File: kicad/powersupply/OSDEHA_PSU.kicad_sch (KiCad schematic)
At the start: 62 parts, among them J1 340 VAC / 220 mA, J10 COLEMANREG-RIGHT-2, J11 HV-L, J12 HV-R, J13 HEATERS-LEFT, J14 HEATERS-RIGHT, J15 Stator bias, J2 340 VAC / 220 mA, J3 420 VAC / 75 mA, J4 9 VAC / 4.5 A, J5 9.5 VAC / 4.5 A, J6 9.5 VAC / 4.5 A, J7 COLEMANREG-LEFT-1, J8 COLEMANREG-LEFT-2, J9 COLEMANREG-RIGHT-1, K1 Relay_DPST-NO, Q1 BD138, Q2 10M90S, U1 LM1085-ADJ, U2 NE555P

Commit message: up
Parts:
- J5, J6: value 9.5 VAC / 4.5 A -> 10.5 VAC / 4.5 A
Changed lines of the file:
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@@
       (effects (font (size 1.27 1.27)) (justify left))
     )
-    (property "Value" "9.5 VAC / 4.5 A" (at 44.45 332.74 0)
+    (property "Value" "10.5 VAC / 4.5 A" (at 44.45 332.74 0)
       (effects (font (size 1.27 1.27)) (justify left))
     )
@@
       (effects (font (size 1.27 1.27)) (justify left))
     )
-    (property "Value" "9.5 VAC / 4.5 A" (at 44.45 351.79 0)
-      (effects (font (size 1.27 1.27)) (justify left))
-    )
+    (property "Value" "10.5 VAC / 4.5 A" (at 44.45 351.79 0)
+      (effects (font (size 1.27 1.27)) (justify left))
+    )

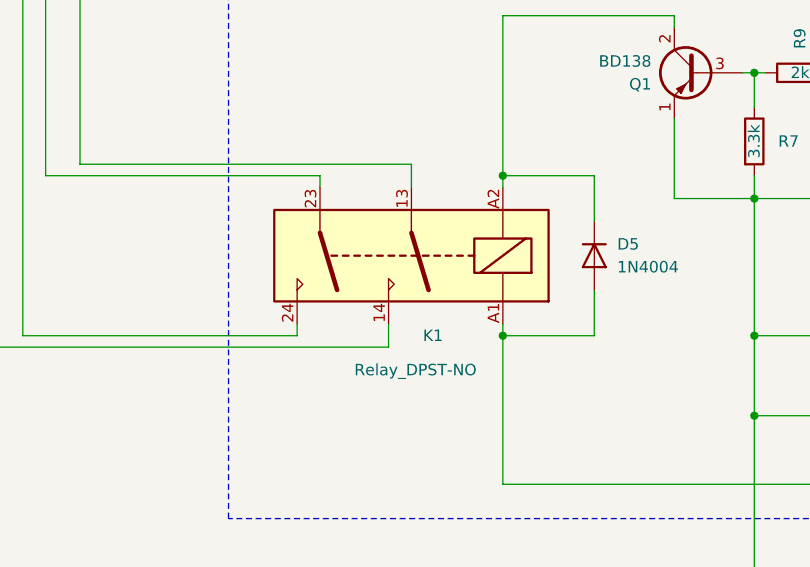
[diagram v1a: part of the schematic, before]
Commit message: fix relay symbol for correct pin numbers
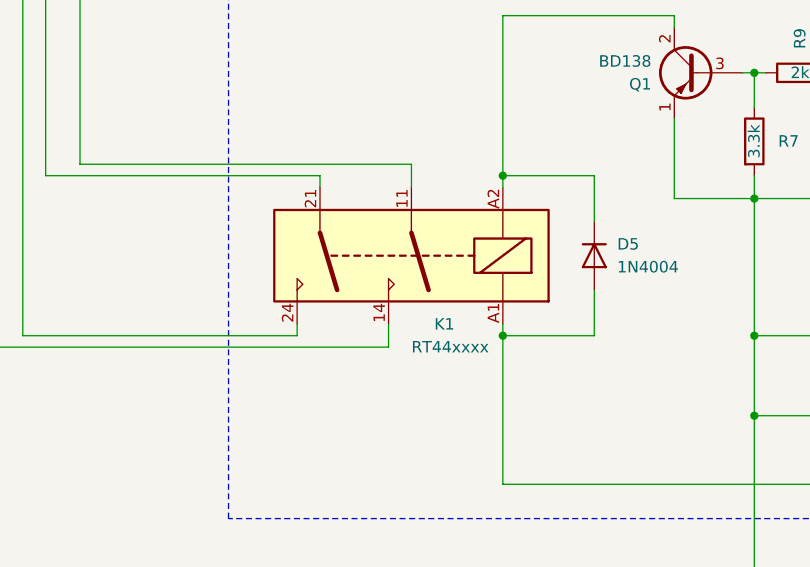
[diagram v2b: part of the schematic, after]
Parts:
- removed K1: Relay_DPST-NO, Relay_THT:Relay_DPST_Schrack-RT2-FormA_RM5mm, symbol Relay:Relay_DPST-NO
- added K1: RT44xxxx, Relay_THT:Relay_DPST_Schrack-RT2-FormA_RM5mm, symbol Relay:RT44xxxx
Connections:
- net GND: now also K1.A1
- net HV_STABI1/AC2: now also K1.11
- net HV_STABI2/AC2: now also K1.21
- net at D5.1 (K), Q1.2 (C): now also K1.A2
- net at J1.2 (Pin_2): now also K1.14
- net at J2.2 (Pin_2): now also K1.24
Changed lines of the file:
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@@
-    )
-  )
-  (symbol (lib_id "Relay:Relay_DPST-NO") (at 99.06 176.53 180) (unit 1)
-    (in_bom yes) (on_board yes) (dnp no)
-    (property "Reference" "K1" (at 100.33 185.42 0)
-      (effects (font (size 1.27 1.27)) (justify right))
-    )
-    (property "Value" "Relay_DPST-NO" (at 92.71 189.23 0)
-      (effects (font (size 1.27 1.27)) (justify right))
-    )
-    (property "Footprint" "Relay_THT:Relay_DPST_Schrack-RT2-FormA_RM5mm" (at 82.55 175.26 0)
-      (effects (font (size 1.27 1.27)) (justify left) hide)
-    )
-    (property "Datasheet" "https://www.mouser.ch/datasheet/2/418/5/product_9_1393243_6_datasheet-1955969.pdf" (at 99.06 176.53 0)
-      (effects (font (size 1.27 1.27)) hide)
-    )
-    (property "MPN" "9-1393243-6" (at 99.06 176.53 0)
-      (effects (font (size 1.27 1.27)) hide)
-    )
-    (pin "14")
-    (pin "13")
-    (pin "23")
-    (pin "A1")
-    (pin "A2")
-    (pin "24")
-    (instances
-      (project "OSDEHA_PSU"
-        (path "/ca37e2fa-48ac-4eb3-a7a4-1e3bbee61661"
-          (reference "K1") (unit 1)
-        )
-      )
     )
   )
@@
         )
       )
+    )
+  )
+  (symbol (lib_id "Relay:RT44xxxx") (at 99.06 176.53 180) (unit 1)
+    (in_bom yes) (on_board yes) (dnp no)
+    (property "Reference" "K1" (at 101.6 184.15 0)
+      (effects (font (size 1.27 1.27)) (justify right))
+    )
+    (property "Value" "RT44xxxx" (at 99.06 186.69 0)
+      (effects (font (size 1.27 1.27)) (justify right))
+    )
+    (property "Footprint" "Relay_THT:Relay_DPST_Schrack-RT2-FormA_RM5mm" (at 99.06 176.53 0)
+      (effects (font (size 1.27 1.27)) hide)
+    )
+    (property "Datasheet" "http://www.te.com/commerce/DocumentDelivery/DDEController?Action=showdoc&DocId=Data+Sheet%7FRT2%7F1014%7Fpdf%7FEnglish%7FENG_DS_RT2_1014.pdf%7F6-1393243-3" (at 99.06 176.53 0)
+      (effects (font (size 1.27 1.27)) hide)
+    )
+    (pin "14")
+    (pin "A2")
+    (pin "A1")
+    (pin "24")
+    (pin "21")
+    (pin "11")
+    (instances
+      (project "OSDEHA_PSU"
+        (path "/ca37e2fa-48ac-4eb3-a7a4-1e3bbee61661"
+          (reference "K1") (unit 1)
+        )
+      )

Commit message: up
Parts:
- removed K1: RT44xxxx, Relay_THT:Relay_DPST_Schrack-RT2-FormA_RM5mm, symbol Relay:RT44xxxx
- added K1: RT424006, Relay_THT:Relay_DPDT_Schrack-RT2-FormC_RM5mm, symbol Relay:RT42xxxx
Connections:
- net GND: now also K1.A1
- net HV_STABI1/AC2: now also K1.11
- net HV_STABI2/AC2: now also K1.21
- net at D5.1 (K), Q1.2 (C): now also K1.A2
- net at J2.2 (Pin_2): now also K1.24
- net at J1.2 (Pin_2): now also K1.14
- no-connect marks 2 -> 4
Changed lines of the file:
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@@
   (junction (at 153.67 194.31) (diameter 0) (color 0 0 0 0)
   )
+  (no_connect (at 91.44 184.15))
   (no_connect (at 153.67 157.48))
+  (no_connect (at 101.6 184.15))
   (no_connect (at 153.67 182.88))
   (wire (pts (xy 137.16 228.6) (xy 137.16 222.25))
@@
         (path "/ca37e2fa-48ac-4eb3-a7a4-1e3bbee61661"
           (reference "J5") (unit 1)
+        )
+      )
+    )
+  )
+  (symbol (lib_id "Relay:RT42xxxx") (at 99.06 176.53 180) (unit 1)
+    (in_bom yes) (on_board yes) (dnp no)
+    (property "Reference" "K1" (at 97.79 186.69 0)
+      (effects (font (size 1.27 1.27)) (justify right))
+    )
+    (property "Value" "RT424006" (at 97.79 189.23 0)
+      (effects (font (size 1.27 1.27)) (justify right))
+    )
+    (property "Footprint" "Relay_THT:Relay_DPDT_Schrack-RT2-FormC_RM5mm" (at 99.06 176.53 0)
+      (effects (font (size 1.27 1.27)) hide)
+    )
+    (property "Datasheet" "http://www.te.com/commerce/DocumentDelivery/DDEController?Action=showdoc&DocId=Data+Sheet%7FRT2%7F1014%7Fpdf%7FEnglish%7FENG_DS_RT2_1014.pdf%7F6-1393243-3" (at 99.06 176.53 0)
+      (effects (font (size 1.27 1.27)) hide)
+    )
+    (property "MPN" "RT424006" (at 99.06 176.53 0)
+      (effects (font (size 1.27 1.27)) hide)
+    )
+    (pin "A2")
+    (pin "14")
+    (pin "12")
+    (pin "11")
+    (pin "A1")
+    (pin "22")
+    (pin "24")
+    (pin "21")
+    (instances
+      (project "OSDEHA_PSU"
+        (path "/ca37e2fa-48ac-4eb3-a7a4-1e3bbee61661"
+          (reference "K1") (unit 1)
         )
       )
@@
         )
       )
-    )
-  )
-  (symbol (lib_id "Relay:RT44xxxx") (at 99.06 176.53 180) (unit 1)
-    (in_bom yes) (on_board yes) (dnp no)
-    (property "Reference" "K1" (at 101.6 184.15 0)
-      (effects (font (size 1.27 1.27)) (justify right))
-    )
-    (property "Value" "RT44xxxx" (at 99.06 186.69 0)
-      (effects (font (size 1.27 1.27)) (justify right))
-    )
-    (property "Footprint" "Relay_THT:Relay_DPST_Schrack-RT2-FormA_RM5mm" (at 99.06 176.53 0)
-      (effects (font (size 1.27 1.27)) hide)
-    )
-    (property "Datasheet" "http://www.te.com/commerce/DocumentDelivery/DDEController?Action=showdoc&DocId=Data+Sheet%7FRT2%7F1014%7Fpdf%7FEnglish%7FENG_DS_RT2_1014.pdf%7F6-1393243-3" (at 99.06 176.53 0)
-      (effects (font (size 1.27 1.27)) hide)
-    )
-    (pin "14")
-    (pin "A2")
-    (pin "A1")
-    (pin "24")
-    (pin "21")
-    (pin "11")
-    (instances
-      (project "OSDEHA_PSU"
-        (path "/ca37e2fa-48ac-4eb3-a7a4-1e3bbee61661"
-          (reference "K1") (unit 1)
-        )
-      )

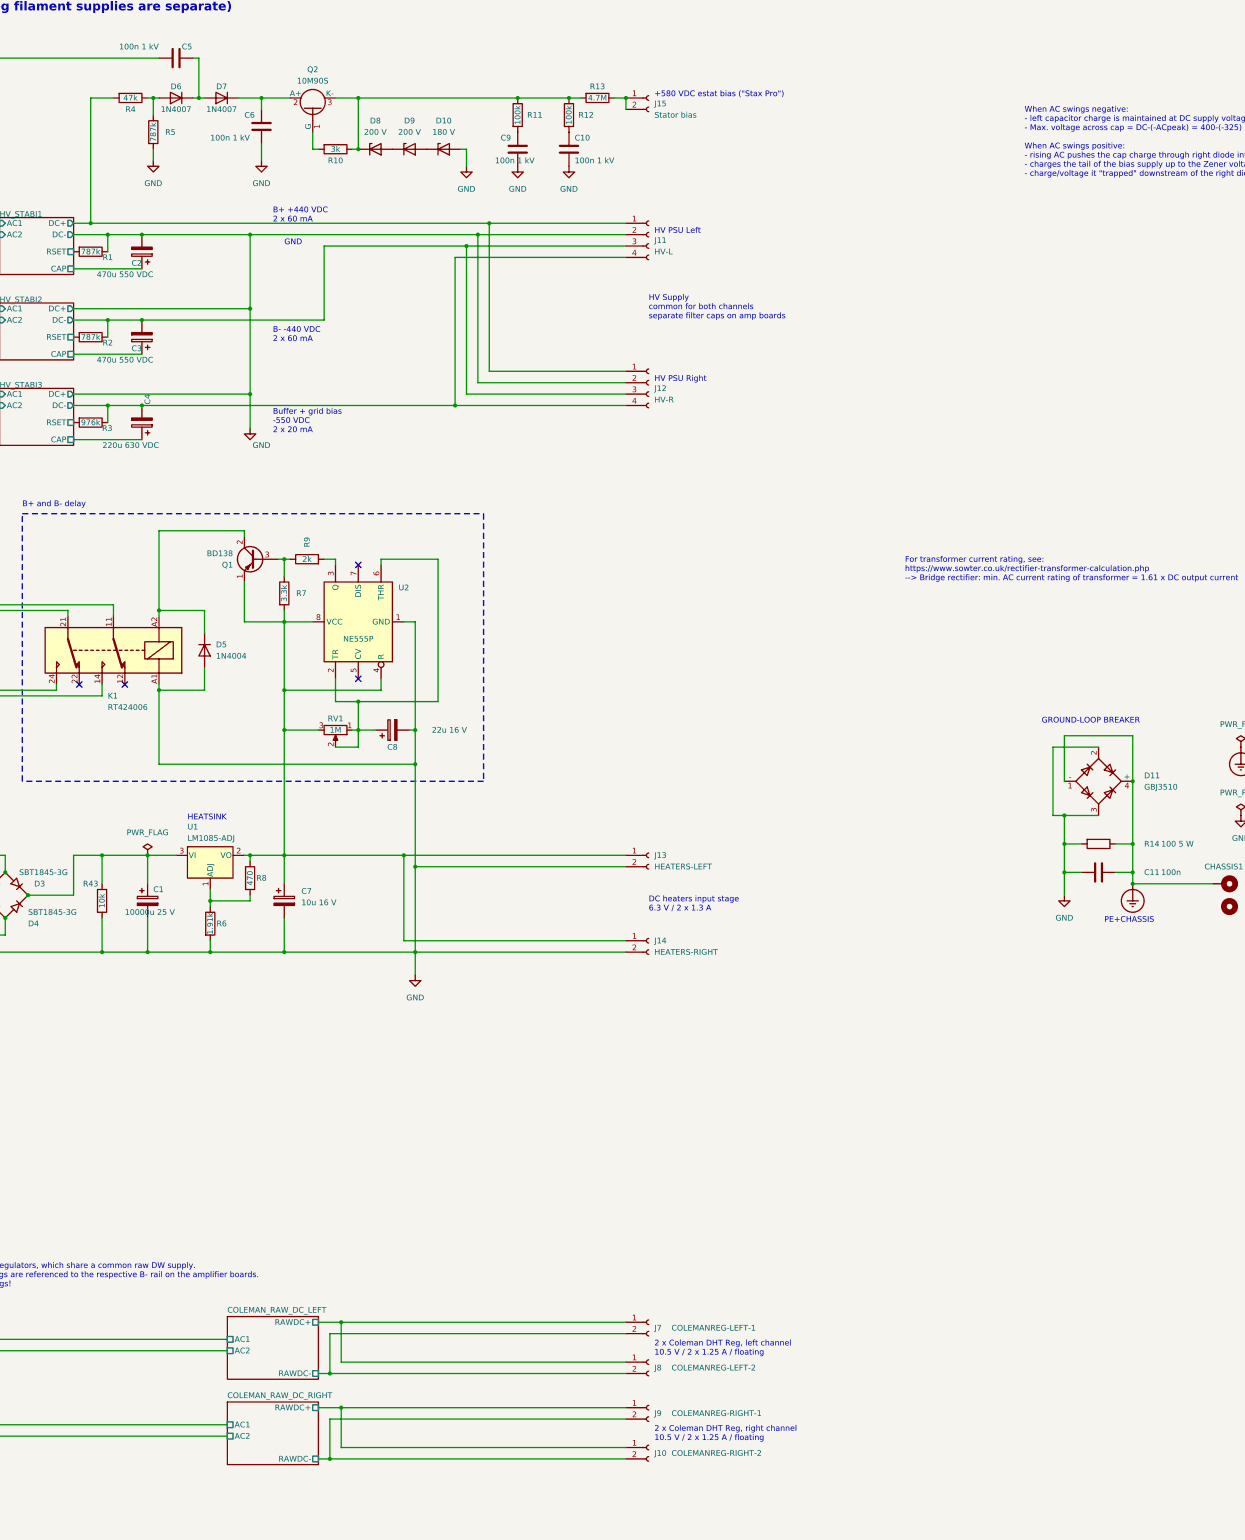
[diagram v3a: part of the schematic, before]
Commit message: psu (del buffer, change output pass part)
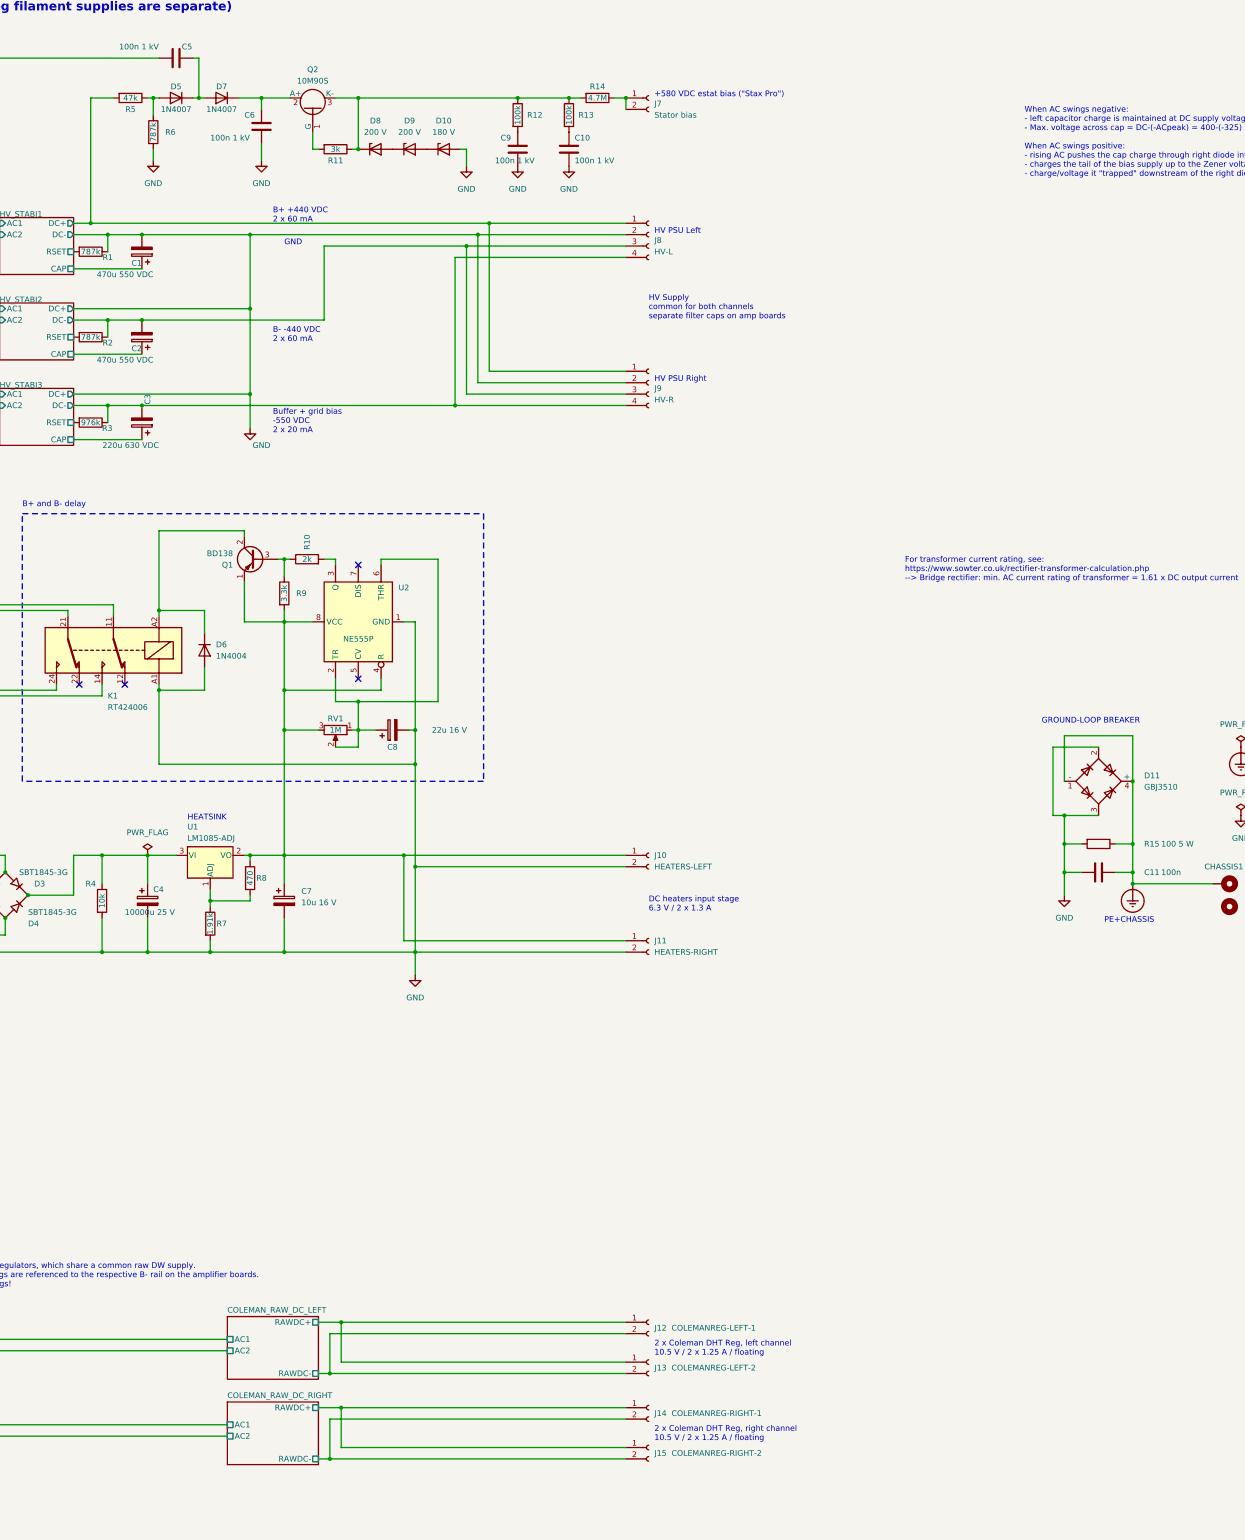
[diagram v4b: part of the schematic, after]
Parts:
- renumbered C2 to C1, C3 to C2, C4 to C3, C1 to C4, D6 to D5, D5 to D6, J13 to J10, J14 to J11, J7 to J12, J8 to J13, J9 to J14, J10 to J15, J15 to J7, J11 to J8, J12 to J9, R9 to R10, R10 to R11, R11 to R12, R12 to R13, R13 to R14, R14 to R15, R43 to R4, R4 to R5, R5 to R6, R6 to R7, R7 to R9

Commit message: psu
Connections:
- net HV_STABI2/AC1: now also J2.2 (Pin_2); no longer J2.1 (Pin_1)
- net at K1.24: now also J2.1 (Pin_1); no longer J2.2 (Pin_2)
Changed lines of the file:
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@@
+    )
+  )
+  (symbol (lib_id "Connector:Screw_Terminal_01x02") (at 38.1 102.87 180) (unit 1)
+    (in_bom yes) (on_board yes) (dnp no)
+    (property "Reference" "J2" (at 35.56 100.33 0)
+      (effects (font (size 1.27 1.27)) (justify left))
+    )
+    (property "Value" "340 VAC / 220 mA" (at 35.56 102.87 0)
+      (effects (font (size 1.27 1.27)) (justify left))
+    )
+    (property "Footprint" "TerminalBlock_Phoenix:TerminalBlock_Phoenix_MKDS-1,5-2-5.08_1x02_P5.08mm_Horizontal" (at 38.1 102.87 0)
+      (effects (font (size 1.27 1.27)) hide)
+    )
+    (property "Datasheet" "https://www.phoenixcontact.com/us/products/1729128/pdf" (at 38.1 102.87 0)
+      (effects (font (size 1.27 1.27)) hide)
+    )
+    (property "MPN" "1729128 " (at 38.1 102.87 0)
+      (effects (font (size 1.27 1.27)) hide)
+    )
+    (pin "2")
+    (pin "1")
+    (instances
+      (project "OSDEHA_PSU"
+        (path "/ca37e2fa-48ac-4eb3-a7a4-1e3bbee61661"
+          (reference "J2") (unit 1)
+        )
+      )
     )
   )
@@
         (path "/ca37e2fa-48ac-4eb3-a7a4-1e3bbee61661"
           (reference "#PWR08") (unit 1)
-        )
-      )
-    )
-  )
-  (symbol (lib_id "Connector:Screw_Terminal_01x02") (at 38.1 100.33 0) (mirror y) (unit 1)
-    (in_bom yes) (on_board yes) (dnp no)
-    (property "Reference" "J2" (at 35.56 100.33 0)
-      (effects (font (size 1.27 1.27)) (justify left))
-    )
-    (property "Value" "340 VAC / 220 mA" (at 35.56 102.87 0)
-      (effects (font (size 1.27 1.27)) (justify left))
-    )
-    (property "Footprint" "TerminalBlock_Phoenix:TerminalBlock_Phoenix_MKDS-1,5-2-5.08_1x02_P5.08mm_Horizontal" (at 38.1 100.33 0)
-      (effects (font (size 1.27 1.27)) hide)
-    )
-    (property "Datasheet" "https://www.phoenixcontact.com/us/products/1729128/pdf" (at 38.1 100.33 0)
-      (effects (font (size 1.27 1.27)) hide)
-    )
-    (property "MPN" "1729128 " (at 38.1 100.33 0)
-      (effects (font (size 1.27 1.27)) hide)
-    )
-    (pin "2")
-    (pin "1")
-    (instances
-      (project "OSDEHA_PSU"
-        (path "/ca37e2fa-48ac-4eb3-a7a4-1e3bbee61661"
-          (reference "J2") (unit 1)
         )
       )
@@
     (instances
       (project "OSDEHA_PSU"
-        (path "/ca37e2fa-48ac-4eb3-a7a4-1e3bbee61661" (page "3"))
+        (path "/ca37e2fa-48ac-4eb3-a7a4-1e3bbee61661" (page "2"))
       )
     )
@@
     (instances
       (project "OSDEHA_PSU"
-        (path "/ca37e2fa-48ac-4eb3-a7a4-1e3bbee61661" (page "2"))
-      )
-    )
+        (path "/ca37e2fa-48ac-4eb3-a7a4-1e3bbee61661" (page "3"))
+      )
+    )
